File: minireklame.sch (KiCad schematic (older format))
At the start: 54 parts, among them IC1 ATXMEGA64A4U-A, P1 CONN_01X04, P10 CONN_01X04, P11 CONN_01X04, P12 CONN_01X04, P13 CONN_01X04, P14 CONN_01X04, P15 CONN_01X04, P16 CONN_01X04, P17 Screw_Terminal_1x02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

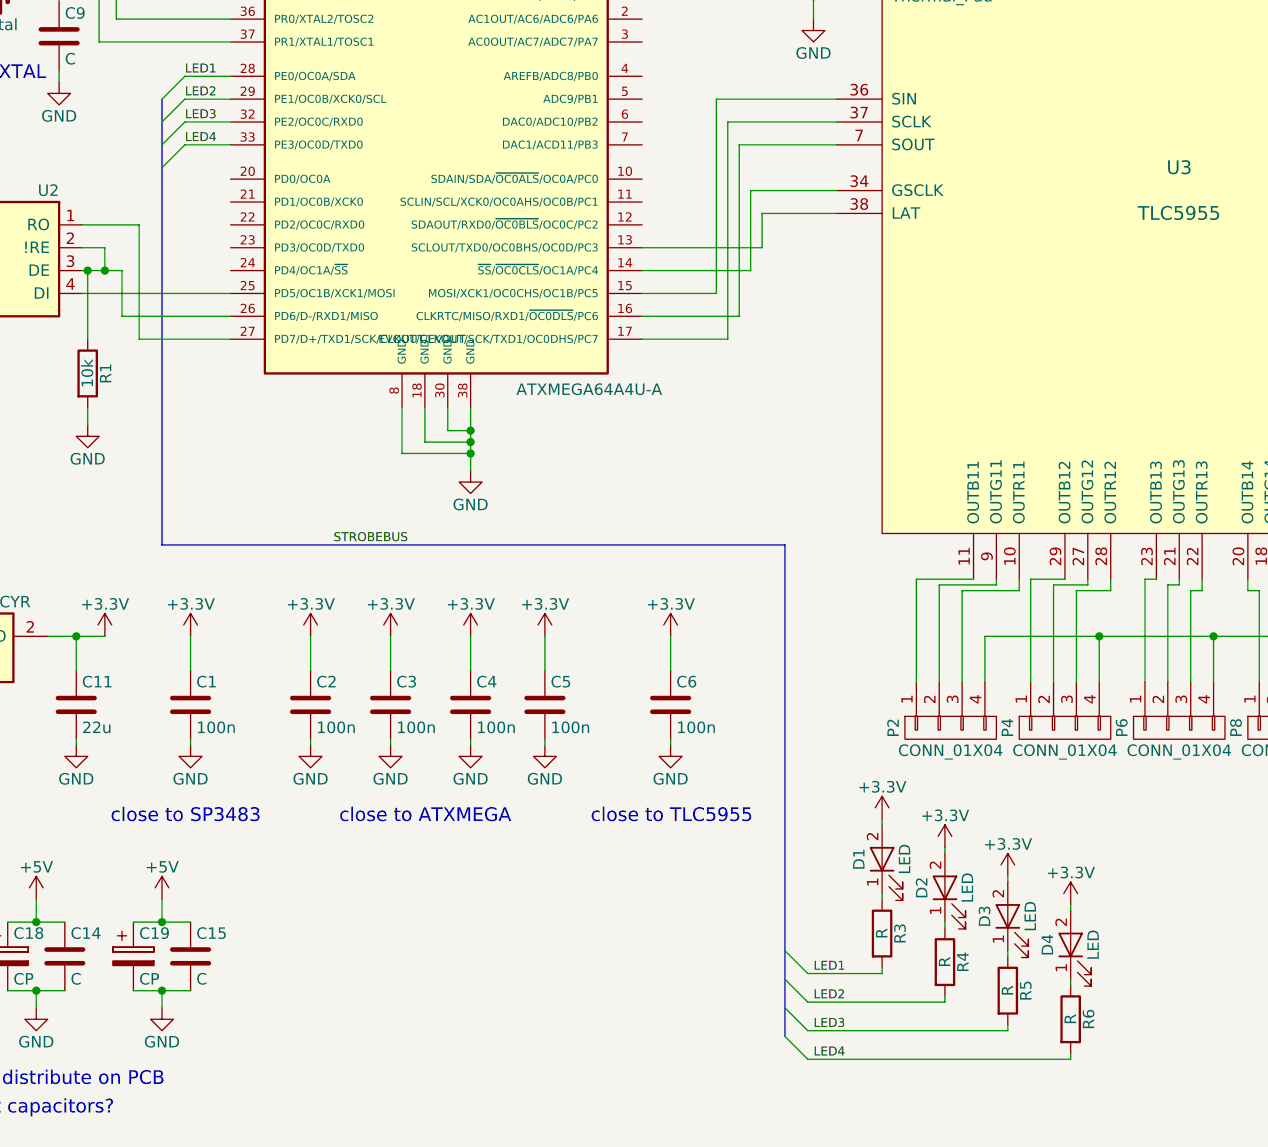
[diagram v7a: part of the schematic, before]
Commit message: adding 4 more LEDs to strobbus, cause we might want to have them too
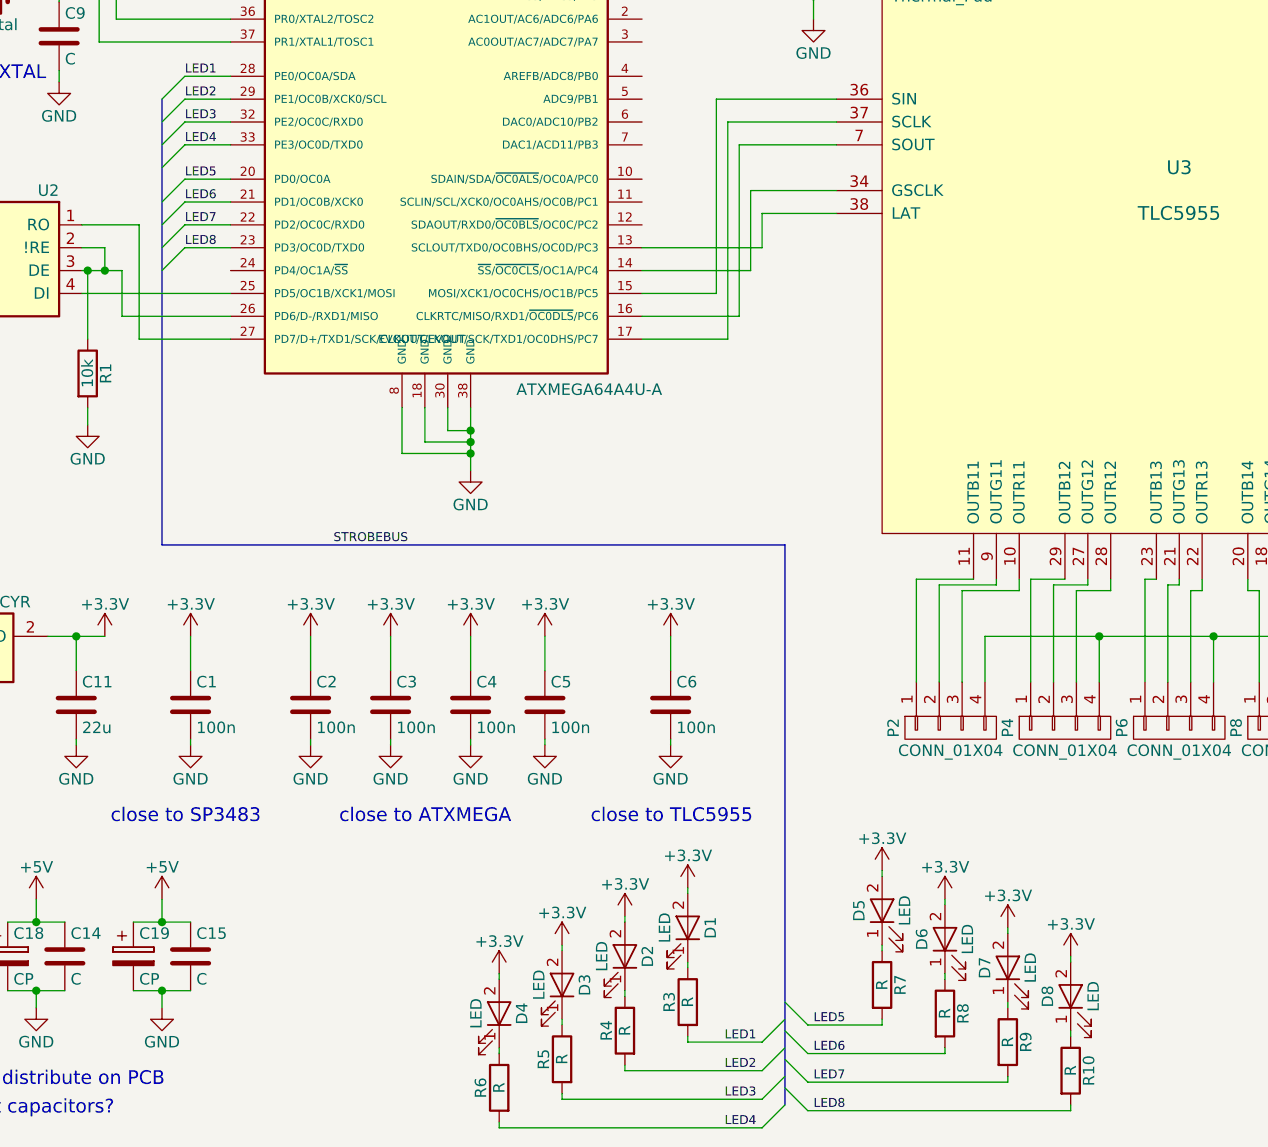
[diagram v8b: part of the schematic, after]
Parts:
- added D5, D6, D7, D8: LED, LEDs:LED_0805, symbol LED
- added R10, R7, R8, R9: R, Resistors_SMD:R_0805_HandSoldering, symbol R
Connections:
- net +3V3: now also D5.2 (A), D6.2 (A), D7.2 (A), D8.2 (A)
- net LED5: now reaches IC1.20 (PD0/OC0A)
- net LED5: now also R7.2
- net LED6: now reaches IC1.21 (PD1/OC0B/XCK0)
- net LED6: now also R8.2
- net LED7: now reaches IC1.22 (PD2/OC0C/RXD0)
- net LED7: now also R9.2
- net LED8: now reaches IC1.23 (PD3/OC0D/TXD0)
- net LED8: now also R10.2
- new net: D5.1 (K), R7.1
- new net: D6.1 (K), R8.1
- new net: D7.1 (K), R9.1
- new net: D8.1 (K), R10.1
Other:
- moved on the sheet: D1, D2, D3, D4, R3, R4, R5, R6
